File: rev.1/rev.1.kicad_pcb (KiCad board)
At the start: 2 copper layers, 100 x 100 mm, 129 parts, among them Q1 BC857, Q2 BC817, SW1 RESET, SW2 POWER, X1 POWER, X2 Манипулятор_1, X3 AUDIO_1, X4 AUDIO_2, X5 Манипулятор_2, X6 VIDEO

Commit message: раставил элементы приступил к трассеровке
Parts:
- moved R18 206.5 mm to (28.1, 72.2), turned to -90 degrees
- moved SW1 195.1 mm to (33.6, 145.1), turned to 90 degrees
- moved R17 193.5 mm to (29.7, 72.2), turned to -90 degrees
- moved R1 192.7 mm to (37.5, 132.7), turned to 90 degrees
- moved C1 189.2 mm to (35.7, 132.7), turned to 90 degrees
- moved L12 188.0 mm to (26.2, 78.8), turned to -90 degrees
- moved R16 187.3 mm to (31.4, 72.2), turned to -90 degrees
- moved R15 187.2 mm to (33.1, 72.2), turned to -90 degrees
- moved R13 183.5 mm to (34.7, 72.2), turned to -90 degrees
- moved R22 178.4 mm to (41.5, 60.5), turned to -90 degrees
- moved R9 176.5 mm to (36.3, 72.2), turned to 90 degrees
- moved R19 175.2 mm to (49.0, 69.5), turned to -90 degrees
- moved C5 174.6 mm to (40.8, 135.4), turned to -90 degrees
- moved R10 173.8 mm to (39.5, 72.2), turned to 90 degrees
- moved C25 169.0 mm to (46.0, 61.6)
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
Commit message: Сделал разводку печатной платы
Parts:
- added C10: 0.1uF, Capacitor_SMD:C_0603_1608Metric, B.Cu at (24.2, 59.6)
- added C2: 0.1uF, Capacitor_SMD:C_0603_1608Metric, B.Cu at (37.6, 50.1)
- C23: renamed from C21; footprint Capacitor_THT:CP_Radial_D6.3mm_P2.50mm -> Capacitor_SMD:CP_Elec_4x5.4
- C24: renamed from C22; footprint Capacitor_THT:CP_Radial_D6.3mm_P2.50mm -> Capacitor_SMD:CP_Elec_4x5.4
- C27: renamed from C25; moved to F.Cu
- C28: renamed from C26; footprint Capacitor_THT:CP_Radial_D6.3mm_P2.50mm -> Capacitor_SMD:CP_Elec_4x5.4
- C3: renamed from C2; footprint Capacitor_THT:CP_Radial_D10.0mm_P5.00mm -> Capacitor_SMD:CP_Elec_8x10.5
- C30: renamed from C28; moved to F.Cu
- C31: renamed from C29; moved to F.Cu
- C36: renamed from C34; footprint Capacitor_THT:CP_Radial_D6.3mm_P2.50mm -> Capacitor_SMD:CP_Elec_4x5.4
- C37: renamed from C35; footprint Capacitor_THT:CP_Radial_D6.3mm_P2.50mm -> Capacitor_SMD:CP_Elec_4x5.4
- C41: renamed from C39; footprint Capacitor_THT:CP_Radial_D7.5mm_P2.50mm -> Capacitor_SMD:CP_Elec_8x6.5
- C43: renamed from C41; moved to F.Cu
- C8: renamed from C7; moved to F.Cu
- C9: renamed from C8; footprint Capacitor_THT:CP_Radial_D6.3mm_P2.50mm -> Capacitor_SMD:CP_Elec_8x10.5
- D4: value SS14 -> BAS85; footprint Diode_SMD:D_SMA -> Diode_SMD:D_MiniMELF
- DA2, DD6, DD9, L15, L5, R10, R13, R14, R15, R16, R17, R18, R2, R34, R35, R37, R9: moved to F.Cu
- DD1, DD2: moved to B.Cu
- SW1: footprint Button_Switch_THT:SW_PUSH_6mm_H7.3mm -> Button_Switch_THT:KLS7_P8X8
- SW2: footprint Button_Switch_THT:Nidec_Copal_SH-7010C -> Button_Switch_THT:KLS7_P8X8
- X3, X4, X6: footprint Connector_Audio:rca_red -> Connector_Audio:RCA-105
- moved SW2 116.1 mm to (35.3, 47.7), turned to 90 degrees
- moved L15 94.2 mm to (102.9, 53.6), turned to -90 degrees
- moved C43 91.7 mm to (104.5, 53.6), turned to -90 degrees
- moved C30 84.4 mm to (106.5, 57.3), turned to 0 degrees
- moved C3 83.5 mm to (32.5, 55.9), turned to -90 degrees
- moved C19 83.3 mm to (30.5, 91.8)
- moved L10 83.3 mm to (29.0, 91.8)
- moved DD6 83.1 mm to (31.3, 73.9)
- moved L12 83.0 mm to (106.3, 100.7)
- moved C6 82.1 mm to (108.0, 88.1), turned to 90 degrees
- moved X1 82.1 mm to (27.4, 48.2)
- moved C21 81.3 mm to (34.5, 128.8), turned to 180 degrees
- moved L3 80.7 mm to (108.0, 84.6), turned to -90 degrees
- moved DD9 80.5 mm to (99.9, 60.6), turned to 90 degrees
- moved C25 79.8 mm to (104.7, 100.7)
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- renumbered C9 to C11, C10 to C12, C11 to C13, C12 to C14, C13 to C15, C14 to C16, C15 to C17, C16 to C18, C17 to C19, C18 to C20, C19 to C21, C20 to C22, C23 to C25, C24 to C26, C27 to C29, C30 to C32, C31 to C33, C32 to C34, C33 to C35, C36 to C38, C37 to C39, C3 to C4, C38 to C40, C40 to C42, C42 to C44, C4 to C5, C5 to C6, C6 to C7
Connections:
- SW1 pad 1: GNDD -> unconnected-(SW1-Pad1)
- SW1 pad 2: /RESET -> GNDD
- SW2 pad 1: Net-(D1-K) -> unconnected-(SW2-Pad1)
- SW2 pad 2: Net-(DA1-Vin) -> Net-(D1-K)
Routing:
- net +5V: track 0.00 -> 473.5 mm, vias 0 -> 20
- net GNDD: track 0.00 -> 287.9 mm, vias 0 -> 62
- net /PAD4: track 0.00 -> 188.1 mm, vias 0 -> 4
- net /PA13: track 0.00 -> 162.2 mm, vias 0 -> 4
- net /PAD0: track 0.00 -> 157.1 mm, vias 0 -> 4
- net /PAD5: track 0.00 -> 154.8 mm, vias 0 -> 2
- net /PAD6: track 0.00 -> 144.2 mm, vias 0 -> 4
- net /PAD7: track 0.00 -> 135.2 mm, vias 0 -> 4
- net /D0: track 0.00 -> 135.1 mm, vias 0 -> 6
- net /D1: track 0.00 -> 126.1 mm, vias 0 -> 4
- net /PAD2: track 0.00 -> 125.4 mm, vias 0 -> 4
- net /PA10: track 0.00 -> 123.7 mm
- net /D4: track 0.00 -> 120.3 mm, vias 0 -> 5
- net /D3: track 0.00 -> 119.4 mm, vias 0 -> 4
- net /PA8: track 0.00 -> 119.0 mm, vias 0 -> 2
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- added copper zone on B.Cu, net GNDD
- added copper zone on F.Cu, net GNDD
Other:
- board size 100 x 100 mm -> 90 x 90 mm

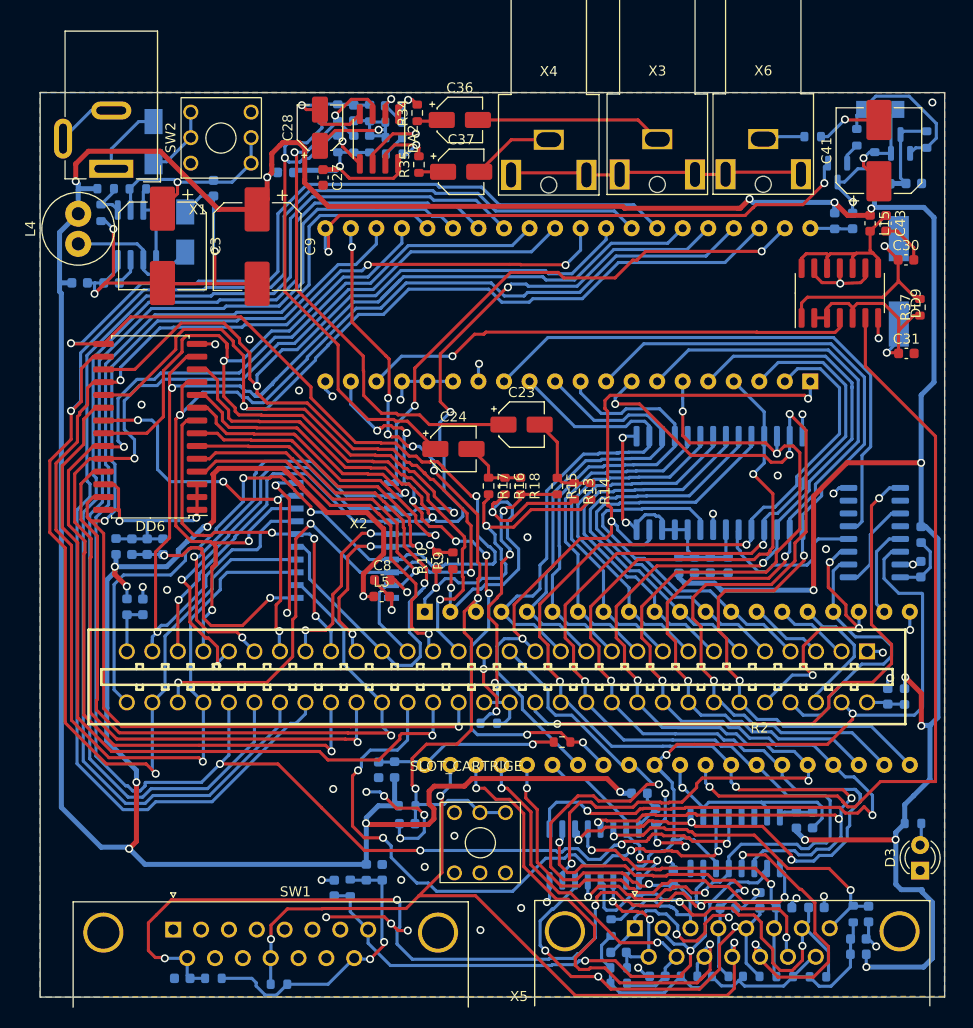
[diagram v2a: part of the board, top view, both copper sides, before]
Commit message: расставил обозначения и надписи
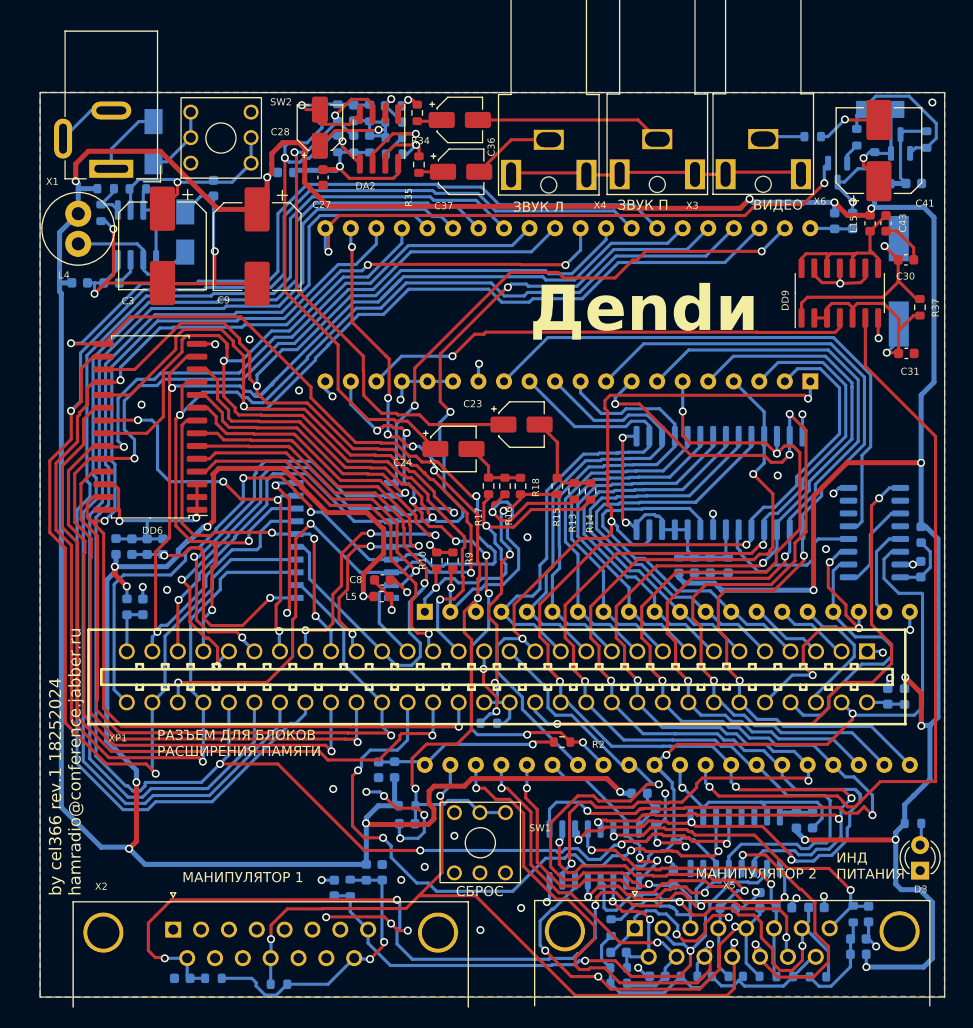
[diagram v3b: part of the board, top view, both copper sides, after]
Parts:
- XP1: value SLOT_CARTRIGE -> ИГРОВОЙ РАЗЪЕМ
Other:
- board text added: "by cel366 rev.1 18252024 hamradio@conference.jabber.ru"
- board text added: "ВИДЕО"
- board text added: "Дendи"
- board text added: "ЗВУК Л"
- board text added: "ЗВУК П"
- board text added: "ИНД ПИТАНИЯ"
- board text added: "МАНИПУЛЯТОР 1"
- board text added: "МАНИПУЛЯТОР 2"
- board text added: "РАЗЪЕМ ДЛЯ БЛОКОВ РАСШИРЕНИЯ ПАМЯТИ"
- board text added: "СБРОС"

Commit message: мелкие улучшения и добавление крепежных отверстий
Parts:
- moved R37 2.66 mm to (105.3, 61.3)
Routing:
- net /PAD2: track 125.4 -> 135.9 mm
- net Net-(DD9-4Y): track 17.5 -> 24.8 mm
- net /PAD3: track 117.3 -> 110.2 mm
- net /PAD1: track 109.5 -> 106.0 mm
- net +5V: track 473.5 -> 470.6 mm, vias 20 -> 18
- net Net-(DD9-1A): track 20.7 -> 18.2 mm
- net Net-(DD9-1Y): track 23.3 -> 20.9 mm
- net /CPU_CLK: track 75.7 -> 77.7 mm
- net /F2: track 74.1 -> 72.1 mm
- net /OUT0: track 78.1 -> 79.8 mm
- net /PA13: track 162.2 -> 163.8 mm
- net /PA5: track 59.8 -> 58.3 mm
- net /PWR: track 112.0 -> 110.8 mm
- net /J2D3: track 42.4 -> 43.4 mm, vias 3 -> 2
- net /D0: track 135.1 -> 134.2 mm
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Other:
- outline, holes or cut-outs redrawn
- board text added: "РАЗЪЕМ ДЛЯ МОДУЛЕЙ ПАМЯТИ"
- board text removed: "РАЗЪЕМ ДЛЯ БЛОКОВ РАСШИРЕНИЯ ПАМЯТИ"

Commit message: добавил список элементов ,гербера
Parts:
- moved C36 85.9 mm to (146.9, 56.9)
- moved C39 85.9 mm to (166.6, 142.1)
- moved C43 85.9 mm to (189.3, 67.1)
- moved C5 85.9 mm to (186.0, 66.9)
- moved DD2 85.9 mm to (181.8, 82.9)
- moved DD4 85.9 mm to (188.1, 97.9)
- moved DD5 85.9 mm to (172.7, 93.0)
- moved DD9 85.9 mm to (184.7, 74.1)
- moved L12 85.9 mm to (191.1, 114.2)
- moved L5 85.9 mm to (139.1, 104.3)
- moved Q1 85.9 mm to (184.5, 62.1)
- moved R12 85.9 mm to (149.8, 116.9)
- moved R13 85.9 mm to (158.3, 93.8)
- moved R22 85.9 mm to (133.2, 56.1)
- moved R23 85.9 mm to (137.9, 59.3)
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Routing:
- net /PA5: track 58.3 -> 60.0 mm
- net /PA7: track 75.4 -> 76.9 mm
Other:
- outline, holes or cut-outs redrawn
- board text added: "rev.1 cel366"

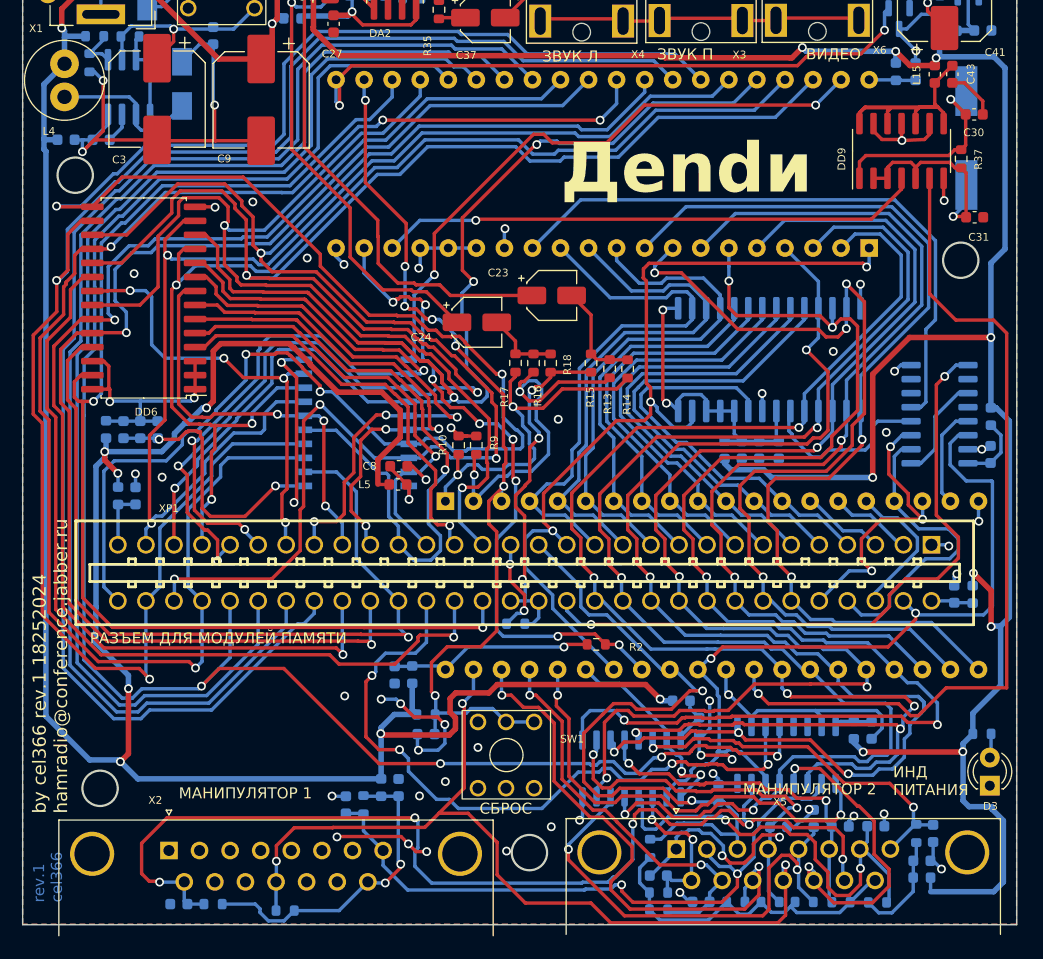
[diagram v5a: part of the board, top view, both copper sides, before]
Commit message: Исправил посадочные места DD5 и DD6 заново сделал файлы svg для ЛУТ , изменил название ревизии rev.1_l
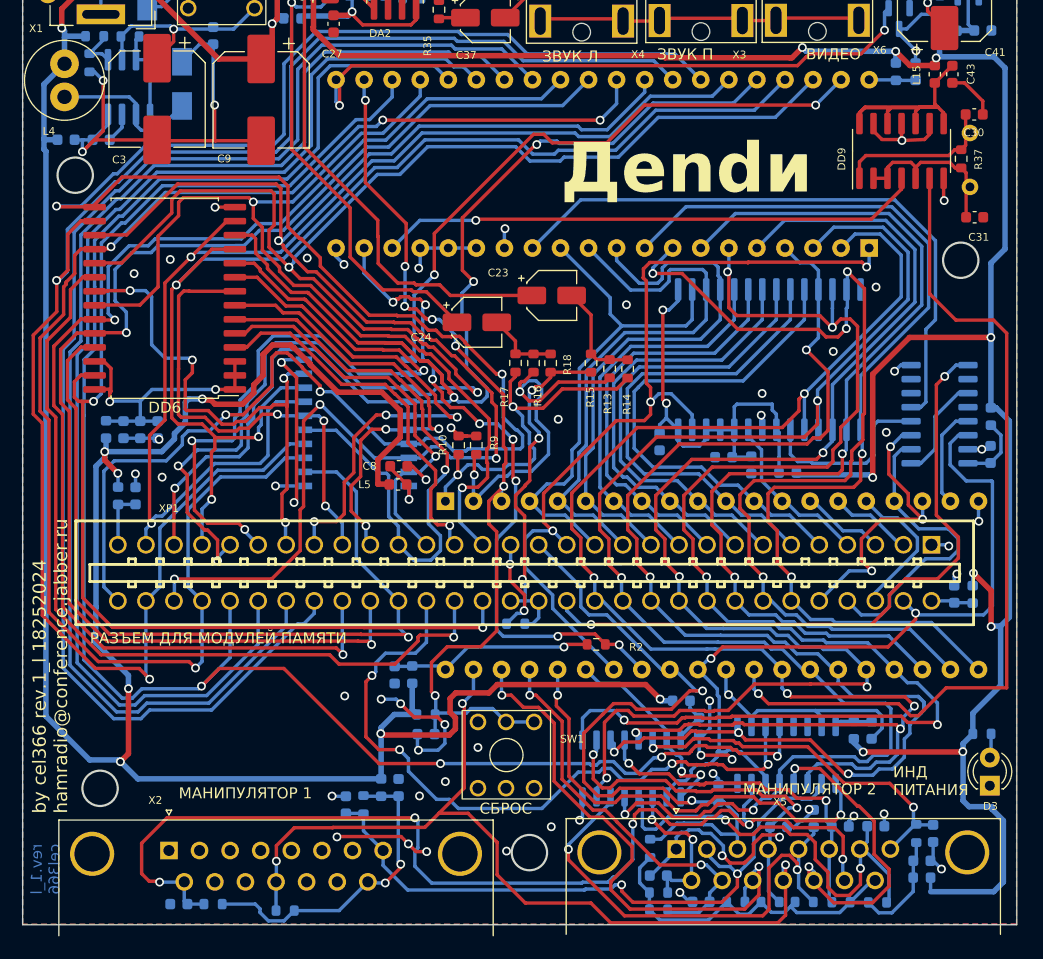
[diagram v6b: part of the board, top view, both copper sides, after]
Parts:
- DD5, DD6: footprint Package_SO:SOIC-28W_7.5x17.9mm_P1.27mm -> Package_SO:SOIC-28L_8.5x17.9mm_P1.27mm
- Z1: footprint Crystal:Crystal_SMD_HC49-SD -> Crystal:Crystal_HC49-4H_Vertical
- moved C12 9.05 mm to (162.8, 100.4)
- moved L6 6.07 mm to (174.4, 103.2), turned to 180 degrees
- moved C13 5.04 mm to (168.6, 101.8), turned to 180 degrees
- moved DD6 1.91 mm to (118.0, 87.4)
- moved C11 1.61 mm to (171.1, 102.5)
- moved Z1 0.56 mm to (190.9, 72.5)
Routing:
- net GNDD: track 287.9 -> 263.0 mm, vias 62 -> 64
- net /A9: track 36.4 -> 15.3 mm
- net Net-(DD5-A10): track 29.7 -> 39.8 mm
- net +5V: track 470.6 -> 463.5 mm
- net /PA1: track 40.7 -> 47.0 mm
- net /PRD: track 94.4 -> 89.1 mm
- net /PA3: track 37.5 -> 42.6 mm
- net /A0: track 50.6 -> 46.5 mm
- net Net-(DD9-1Y): track 20.9 -> 16.7 mm, vias 1 -> 0
- net /A7: track 40.3 -> 44.4 mm
- net /PA2: track 52.4 -> 48.4 mm
- net /A8: track 42.6 -> 46.4 mm
- net /PA5: track 60.0 -> 56.4 mm
- net /PA4: track 46.2 -> 42.6 mm
- net /PA6: track 40.1 -> 36.5 mm
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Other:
- board text added: "by cel366 rev.1_l 18252024 hamradio@conference.jabber.ru"
- board text added: "rev.1_l cel366"
- board text removed: "by cel366 rev.1 18252024 hamradio@conference.jabber.ru"
- board text removed: "rev.1 cel366"
